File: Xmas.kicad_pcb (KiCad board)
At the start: 2 copper layers, 23 parts, among them IC1 STM32C011F6, IC2 TP4056-42, SW1 BZCN_TSA007A1518B03

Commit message: The schematic is complete
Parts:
- added C10: 100n, BornaKiCad:C0603, B.Cu at (108.2, 114.0)
- added C11: DNP, BornaKiCad:C0603, F.Cu at (79.1, 38.9)
- added C12: DNP, BornaKiCad:C0603, F.Cu at (79.1, 41.4)
- added C13: 10n, BornaKiCad:C0603, F.Cu at (79.1, 43.9)
- added C4: 100n, BornaKiCad:C0603, B.Cu at (148.1, 90.2)
- added C5: 100n, BornaKiCad:C0603, B.Cu at (112.5, 97.8)
- added C6: 100n, BornaKiCad:C0603, B.Cu at (137.3, 112.3)
- added C7: 100n, BornaKiCad:C0603, F.Cu at (79.1, 31.4)
- added C8: 10uF, BornaKiCad:C1206, F.Cu at (74.3, 41.6)
- added C9: 100n, BornaKiCad:C0603, B.Cu at (142.7, 114.2)
- added D1: BAT20JFILM, BornaKiCad:SOD323, F.Cu at (91.0, 43.7)
- added Q1: AO3401A, BornaKiCad:SOT-23-3L, F.Cu at (88.1, 47.2)
- added Q2: CJ3400, BornaKiCad:SOT-23-3L, F.Cu at (92.1, 47.2)
- added R10: 10k, BornaKiCad:R0603, B.Cu at (110.5, 113.1)
- added R11: 100k, BornaKiCad:R0603, F.Cu at (87.1, 33.9)
- added R12: 100R, BornaKiCad:R0603, F.Cu at (87.1, 36.4)
- added R13: 100k, BornaKiCad:R0603, F.Cu at (87.1, 38.9)
- added R14: 10R, BornaKiCad:R1206, F.Cu at (74.3, 44.9)
- added R4: 10k, BornaKiCad:R0603, F.Cu at (83.1, 31.4)
- added R5: 10k, BornaKiCad:R0603, F.Cu at (83.1, 33.9)
- added R6: 100R, BornaKiCad:R0603, F.Cu at (83.1, 36.4)
- added R7: 100k, BornaKiCad:R0603, F.Cu at (83.1, 38.9)
- added R8: 100k, BornaKiCad:R0603, F.Cu at (83.1, 41.4)
- added R9: 10k, BornaKiCad:R0603, B.Cu at (140.7, 113.5)
- added SPK1: MLT-7525, BornaKiCad:MTL-7525, B.Cu at (144.9, 79.8)
- added SW2: BZCN_TSA007A1518B03, BornaKiCad:TSA007A1518B03, F.Cu at (102.8, 115.3)
- added TP1: ~, BornaKiCad:TP-1_5mm, F.Cu at (90.4, 31.4)
- added TP2: ~, BornaKiCad:TP-1_5mm, F.Cu at (90.4, 33.9)
- added TP3: ~, BornaKiCad:TP-1_5mm, F.Cu at (90.4, 36.4)
- added TP4: ~, BornaKiCad:TP-1_5mm, F.Cu at (90.4, 38.9)
- added TP5: ~, BornaKiCad:TP-1_5mm, F.Cu at (90.4, 41.4)
- C1: value VALUE -> 100n; footprint BornaKiCad:C1206 -> BornaKiCad:C0603; moved to B.Cu
- C2, C3: value 2u2 -> 100n
- CONN1, CONN2, IC1: moved to B.Cu
- R1, R2: value VALUE -> 5k1
- R3: value 2k2 -> 10k
- moved SW1 79.8 mm to (147.2, 115.3), turned to -60 degrees
- moved C1 79.6 mm to (105.0, 83.0)
- moved CONN1 72.2 mm to (135.1, 97.8), turned to 90 degrees
- moved CONN2 66.5 mm to (125.0, 108.5)
- moved IC1 56.4 mm to (116.7, 83.8), turned to 180 degrees
- moved C2 8.16 mm to (48.5, 81.1)
- moved C3 4.85 mm to (53.5, 77.7)
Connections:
- net /DO renamed Net-(LED4-DO)
- net /DO2 renamed Net-(LED8-DO)
- net VBAT renamed VDD
- C1 pad 1: /DIN -> GND
- C1 pad 2: Net-(LED1-DI) -> WS_SUPPLY
- CONN2 pad A6: unconnected-(CONN2-DP1-PadA6) -> Net-(CONN2-DP1)
- CONN2 pad A7: unconnected-(CONN2-DN1-PadA7) -> Net-(CONN2-DN1)
- CONN2 pad B6: unconnected-(CONN2-DP2-PadB6) -> Net-(CONN2-DP1)
- CONN2 pad B7: unconnected-(CONN2-DN2-PadB7) -> Net-(CONN2-DN1)
- IC1 pad 12: unconnected-(IC1-PA5-Pad12) -> /BUZZER
- IC1 pad 13: unconnected-(IC1-PA6-Pad13) -> /DIN
- IC1 pad 14: unconnected-(IC1-PA7-Pad14) -> /PERIPH_SUPPLY
- IC1 pad 18: unconnected-(IC1-PA13-Pad18) -> /SW_DIO
- IC1 pad 19: unconnected-(IC1-BOOT0-Pad19) -> /SW_CLK
- IC1 pad 20: /DIN -> unconnected-(IC1-PB6-Pad20)
- IC1 pad 6: unconnected-(IC1-NRST-Pad6) -> /RST
- IC1 pad 7: unconnected-(IC1-PA0-Pad7) -> /BTN2
- IC1 pad 9: unconnected-(IC1-PA2-Pad9) -> /BTN1
- IC2 pad 1: TEMP -> Net-(IC2-TEMP)
- IC2 pad 2: PROG -> Net-(IC2-PROG)
- LED1 pad 3: Net-(LED1-DI) -> /DIN
- LED1 pad 4: unconnected-(LED1-VDD-Pad4) -> WS_SUPPLY
- LED10 pad 4: unconnected-(LED10-VDD-Pad4) -> WS_SUPPLY
- LED11 pad 4: unconnected-(LED11-VDD-Pad4) -> WS_SUPPLY
- LED12 pad 4: unconnected-(LED12-VDD-Pad4) -> WS_SUPPLY
- LED2 pad 4: unconnected-(LED2-VDD-Pad4) -> WS_SUPPLY
- LED3 pad 4: unconnected-(LED3-VDD-Pad4) -> WS_SUPPLY
- LED4 pad 4: unconnected-(LED4-VDD-Pad4) -> WS_SUPPLY
- LED5 pad 4: unconnected-(LED5-VDD-Pad4) -> WS_SUPPLY
- LED6 pad 4: unconnected-(LED6-VDD-Pad4) -> WS_SUPPLY
- LED7 pad 4: unconnected-(LED7-VDD-Pad4) -> WS_SUPPLY
- LED8 pad 4: unconnected-(LED8-VDD-Pad4) -> WS_SUPPLY
- LED9 pad 4: unconnected-(LED9-VDD-Pad4) -> WS_SUPPLY
- SW1 pad 1: unconnected-(SW1-SW1-Pad1) -> GND
- SW1 pad 2: unconnected-(SW1-SW2-Pad2) -> /BTN1
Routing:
- net /BTN1: track 0.00 -> 65.8 mm, vias 0 -> 2
- net /BTN2: track 0.00 -> 54.0 mm, vias 0 -> 2
- net Net-(LED3-DO): track 50.2 -> 26.2 mm, vias 0 -> 2
- net GND: track 0.00 -> 21.0 mm, vias 0 -> 4
- net WS_SUPPLY: track 0.00 -> 18.7 mm, vias 0 -> 4
- net Net-(LED10-DI): track 18.5 -> 25.7 mm, vias 0 -> 2
- net Net-(LED11-DO): track 35.2 -> 29.7 mm
- net Net-(LED7-DO): track 30.1 -> 26.7 mm
- net Net-(LED6-DO): track 56.3 -> 53.3 mm, vias 0 -> 4
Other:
- board outline added: 50 x 60.6 mm

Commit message: Update PCB
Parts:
- moved CONN2 5.55 mm to (130.5, 109.1), turned to 180 degrees
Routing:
- net Net-(LED3-DO): track 26.2 -> 45.2 mm, vias 2 -> 4
- net /BTN1: track 65.8 -> 58.0 mm, vias 2 -> 1
- net /BTN2: track 54.0 -> 49.3 mm, vias 2 -> 1
- net GND: track 21.0 -> 19.2 mm
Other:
- outline, holes or cut-outs redrawn

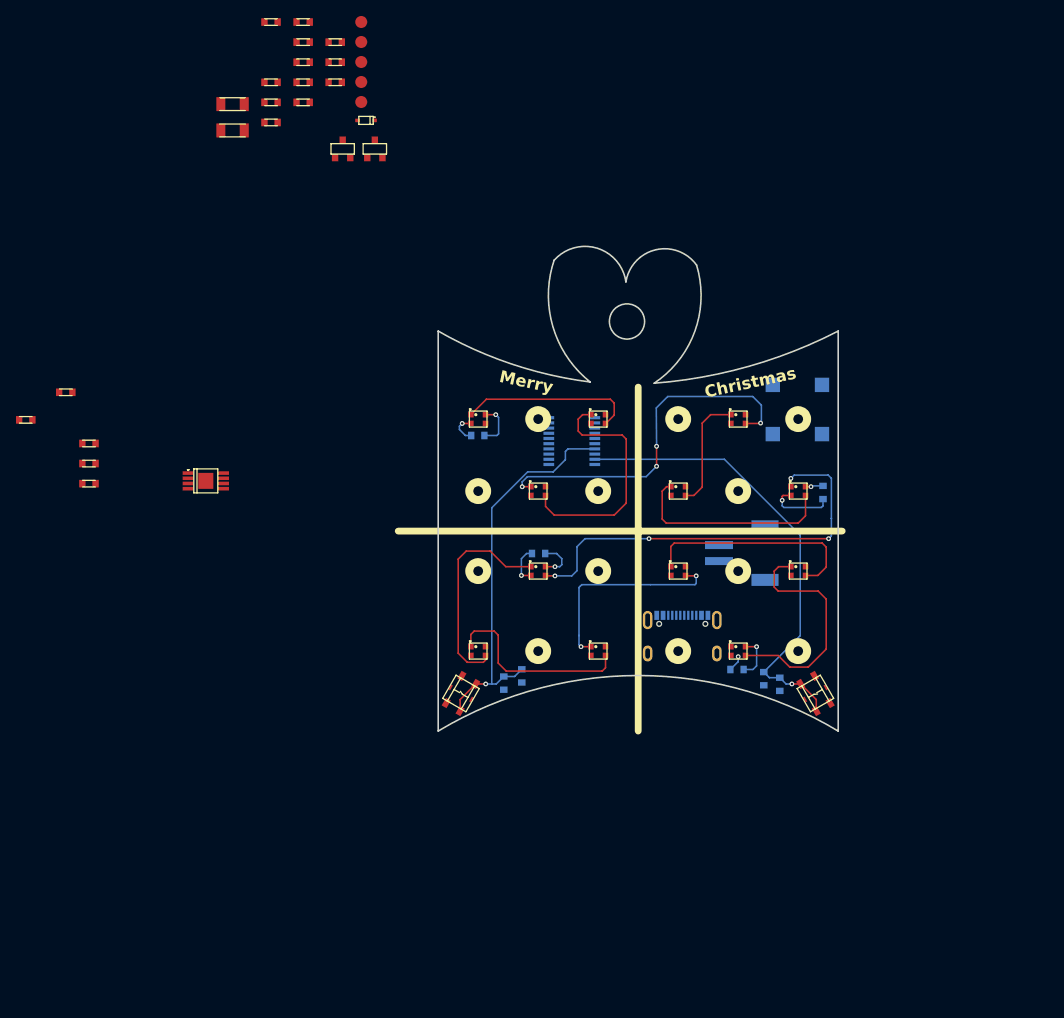
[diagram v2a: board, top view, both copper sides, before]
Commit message: Everything on the PCB is connected
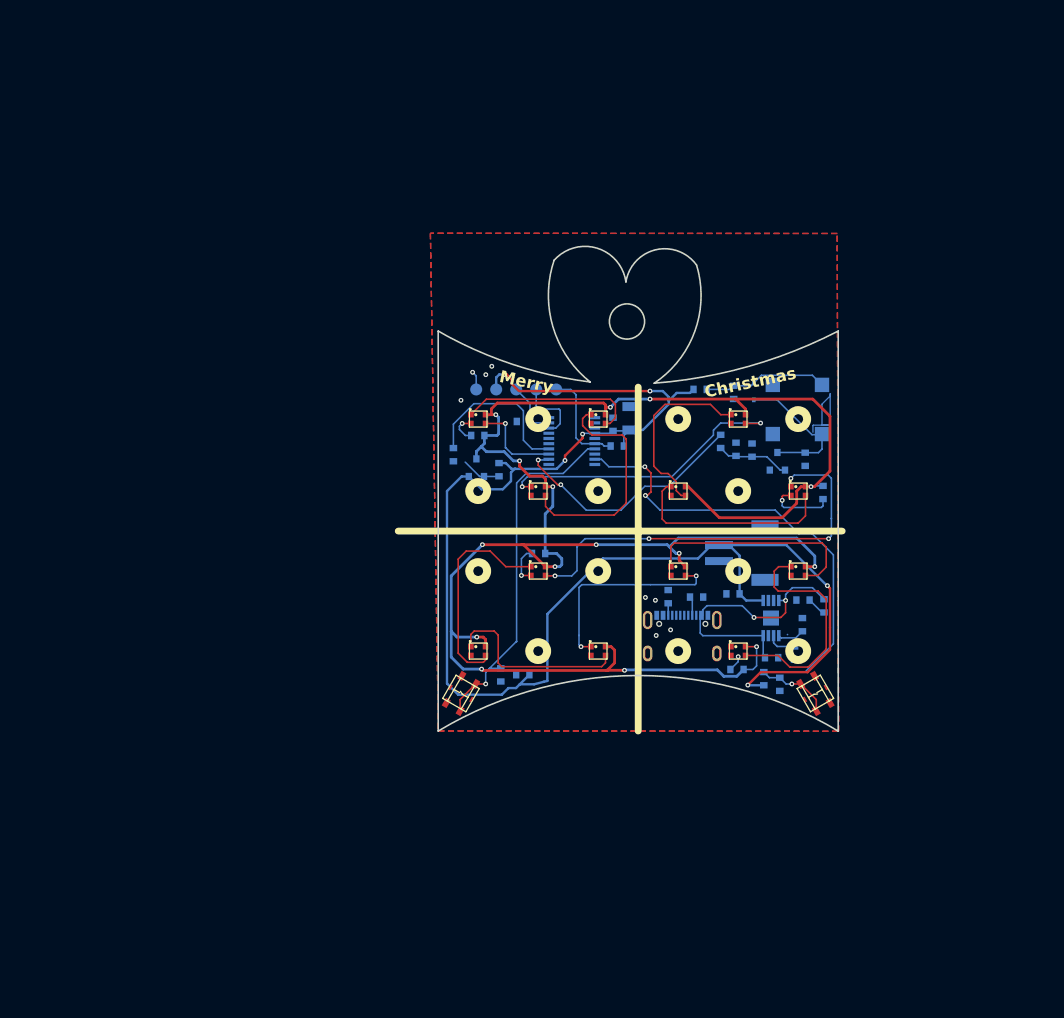
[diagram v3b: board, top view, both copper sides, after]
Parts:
- added LED13: ~, BornaKiCad:LED_0603, B.Cu at (148.2, 104.4)
- C11, C12, C13, C2, C3, C7, C8, D1, IC2, Q1, Q2, R1, R11, R12, R13, R2, R3, R4, R5, R6, R7, R8, TP1, TP2, TP3, TP4, TP5: moved to B.Cu
- R14: footprint BornaKiCad:R1206 -> BornaKiCad:R0603; moved to B.Cu
- moved R4 100.0 mm to (144.6, 110.2), turned to 90 degrees
- moved C2 97.8 mm to (141.7, 110.8), turned to 180 degrees
- moved R5 95.9 mm to (145.5, 106.7), turned to -90 degrees
- moved R3 90.4 mm to (145.6, 103.6)
- moved C3 87.1 mm to (136.8, 102.8)
- moved C12 80.3 mm to (145.9, 86.0), turned to 90 degrees
- moved R1 78.3 mm to (132.3, 103.2)
- moved R2 74.3 mm to (128.8, 103.2), turned to 90 degrees
- moved C11 74.0 mm to (137.2, 84.8), turned to -90 degrees
- moved IC2 72.7 mm to (141.6, 105.9), turned to 90 degrees
- moved R13 69.5 mm to (139.2, 84.9), turned to -90 degrees
- moved R12 67.6 mm to (135.3, 83.8), turned to -90 degrees
- moved C13 66.9 mm to (136.9, 77.7), turned to 90 degrees
- moved R14 66.8 mm to (132.7, 77.3), turned to 180 degrees
- moved C7 66.0 mm to (121.8, 81.7), turned to -90 degrees
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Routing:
- net WS_SUPPLY: track 18.7 -> 238.2 mm, vias 4 -> 15
- net VDD: track 0.00 -> 190.7 mm, vias 0 -> 6
- net VUSB: track 0.00 -> 34.1 mm, vias 0 -> 2
- net /BUZZER: track 0.00 -> 31.1 mm, vias 0 -> 2
- net Net-(Q2-D): track 0.00 -> 20.6 mm
- net /PERIPH_SUPPLY: track 0.00 -> 20.5 mm
- net Net-(C13-Pad2): track 0.00 -> 15.9 mm
- net (no net): track 0.00 -> 12.9 mm
- net /RST: track 0.00 -> 12.9 mm
- net /DIN: track 0.00 -> 11.3 mm, vias 0 -> 1
- net /BTN1: track 58.0 -> 68.5 mm, vias 1 -> 3
- net Net-(Q2-G): track 0.00 -> 9.18 mm
- net Net-(LED4-DO): track 14.5 -> 23.2 mm
- net /SW_DIO: track 0.00 -> 8.61 mm
- net Net-(LED3-DO): track 45.2 -> 36.9 mm, vias 4 -> 2
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- added copper zone on B.Cu, net GND
- added copper zone on F.Cu, net GND

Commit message: Update PCB
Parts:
- moved R10 8.09 mm to (103.2, 109.8)
- moved R9 7.77 mm to (147.7, 110.0), turned to 90 degrees
- moved LED13 3.65 mm to (145.6, 101.9), turned to 0 degrees
- moved R6 3.04 mm to (104.8, 84.7), turned to 0 degrees
- moved C10 2.82 mm to (105.2, 112.0), turned to 180 degrees
- moved R12 2.07 mm to (134.3, 85.6), turned to 0 degrees
- moved C9 1.40 mm to (142.6, 112.8), turned to 0 degrees
- moved R11 0.66 mm to (108.2, 87.2), turned to -90 degrees
- moved Q1 0.40 mm to (105.2, 87.2), turned to -90 degrees
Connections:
- IC1 pad 11: unconnected-(IC1-PA4-Pad11) -> /BTN2
- IC1 pad 7: /BTN2 -> unconnected-(IC1-PA0-Pad7)
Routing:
- net VDD: track 190.7 -> 163.0 mm, vias 6 -> 2
- net WS_SUPPLY: track 238.2 -> 213.8 mm, vias 15 -> 13
- net /BUZZER: track 31.1 -> 25.9 mm
- net /BTN1: track 68.5 -> 63.8 mm
- net VUSB: track 34.1 -> 29.8 mm
- net Net-(Q1-G): track 4.98 -> 1.79 mm
- net /BTN2: track 45.5 -> 43.6 mm
- net Net-(Q2-D): track 20.6 -> 21.7 mm
- net /RST: track 12.9 -> 11.8 mm
- net GND: track 21.5 -> 20.6 mm, vias 12 -> 57
- net Net-(LED3-DO): track 36.9 -> 36.2 mm
- net Net-(LED11-DO): track 29.3 -> 28.6 mm
- net Net-(LED13-K): track 2.44 -> 1.76 mm
- net /PERIPH_SUPPLY: track 20.5 -> 21.1 mm

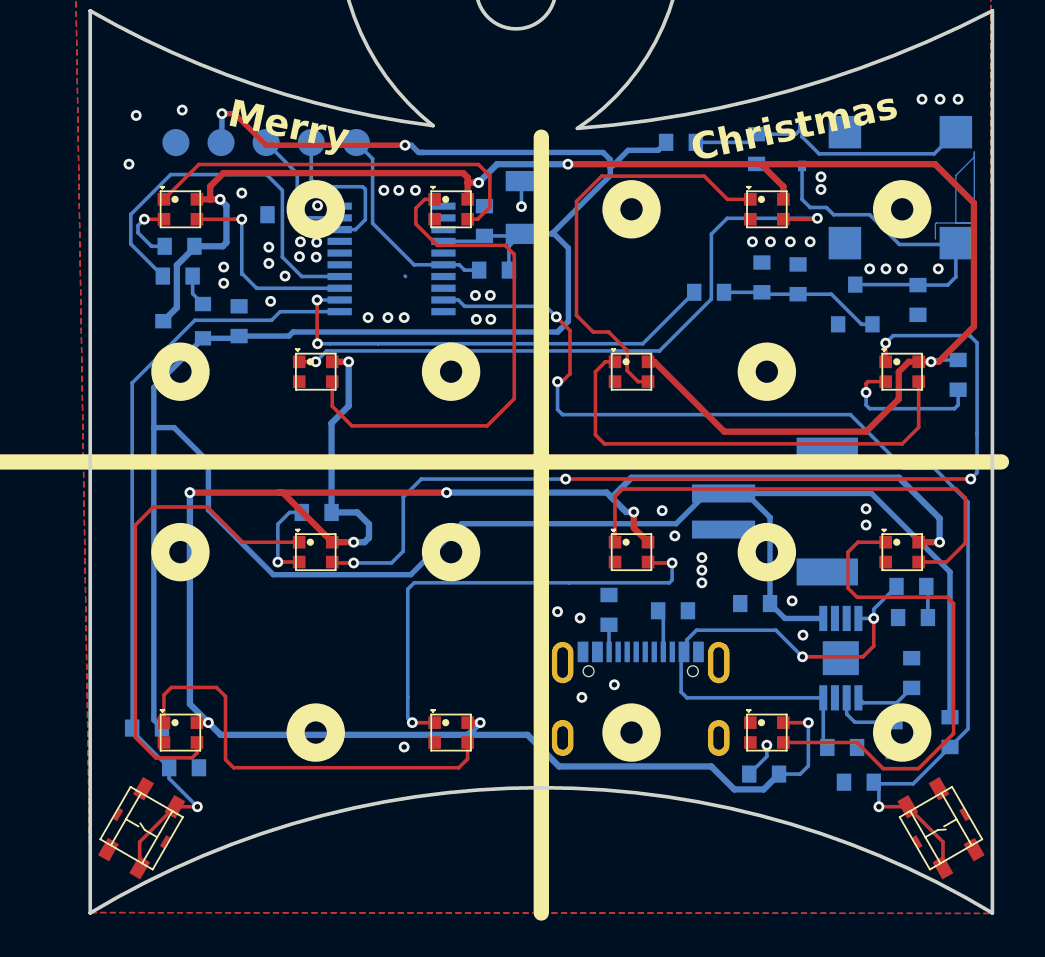
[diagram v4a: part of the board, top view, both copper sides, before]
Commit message: Connected uncotected traces/Marina
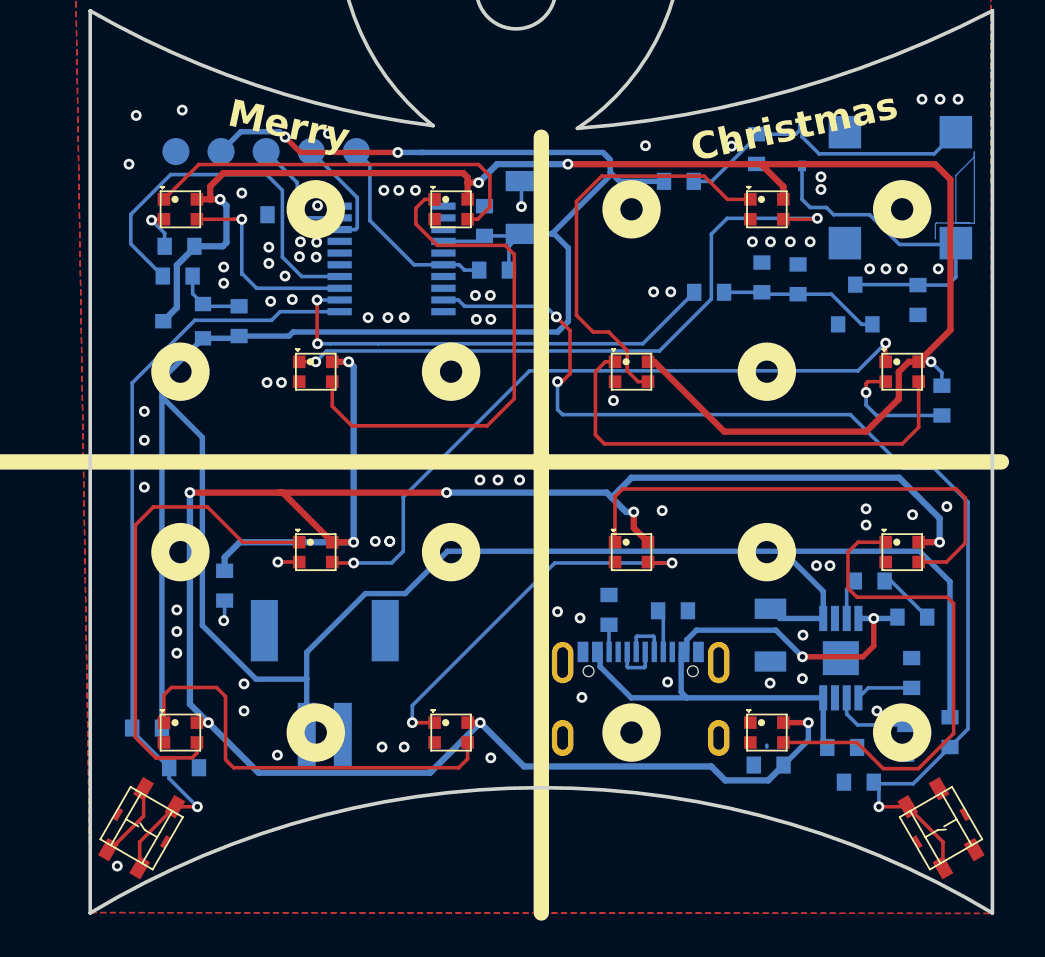
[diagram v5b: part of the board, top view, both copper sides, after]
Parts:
- C3: value 100n -> 10u; footprint BornaKiCad:C0603 -> Borna KiCAD Library:C1206
- moved CONN1 25.3 mm to (113.0, 110.1), turned to 180 degrees
- moved C5 6.52 mm to (107.5, 101.9), turned to 90 degrees
- moved R3 3.14 mm to (143.2, 101.6)
- moved R14 2.16 mm to (132.6, 79.5)
- moved C3 1.95 mm to (137.7, 104.6), turned to 90 degrees
- moved LED13 1.70 mm to (145.6, 103.6)
- moved C4 1.69 mm to (147.2, 91.6)
- moved R4 0.67 mm to (145.2, 110.4)
- moved C6 0.56 mm to (137.6, 111.8)
- moved TP1 0.50 mm to (104.8, 77.8)
- moved TP2 0.50 mm to (107.2, 77.8)
- moved TP3 0.50 mm to (109.8, 77.8)
- moved TP4 0.50 mm to (112.2, 77.8)
- moved TP5 0.50 mm to (114.8, 77.8)
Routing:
- net Net-(LED6-DO): track 53.3 -> 38.5 mm, vias 4 -> 2
- net VUSB: track 29.8 -> 35.2 mm
- net VDD: track 163.0 -> 167.8 mm
- net Net-(LED10-DI): track 25.7 -> 21.2 mm
- net WS_SUPPLY: track 213.8 -> 217.7 mm
- net GND: track 20.6 -> 17.2 mm, vias 57 -> 86
- net Net-(CONN2-DN1): track 0.00 -> 2.68 mm
- net Net-(CONN2-DP1): track 0.00 -> 2.68 mm
- net /SW_DIO: track 8.61 -> 6.30 mm
- net Net-(IC2-CHRG): track 0.00 -> 2.26 mm
- net Net-(Q1-G): track 1.79 -> 3.84 mm
- net Net-(LED13-K): track 1.76 -> 3.19 mm
- net Net-(C13-Pad2): track 16.4 -> 17.4 mm
- net Net-(IC2-PROG): track 3.71 -> 4.42 mm
- net /RST: track 11.8 -> 11.3 mm
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
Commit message: Fixed paths in project files.
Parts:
- C1, C10, C11, C12, C13, C2, C4, C5, C6, C7, C9: footprint BornaKiCad:C0603 -> Borna KiCAD Library:C0603
- C8: footprint BornaKiCad:C1206 -> Borna KiCAD Library:C1206
- CONN1: footprint BornaKiCad:JST_S2B-PH-SM4-TB -> Borna KiCAD Library:JST_S2B-PH-SM4-TB
- CONN2: footprint BornaKiCad:TYPE-C_16PIN_2MD(073) -> Borna KiCAD Library:TYPE-C_16PIN_2MD(073)
- D1: footprint BornaKiCad:SOD323 -> Borna KiCAD Library:SOD323
- IC1: footprint BornaKiCad:TSSOP20 -> Borna KiCAD Library:TSSOP20
- IC2: footprint BornaKiCad:EMSOP -> Borna KiCAD Library:EMSOP
- LED1, LED10, LED11, LED12, LED2, LED3, LED4, LED5, LED6, LED7, LED8, LED9: footprint BornaKiCad:WS2812B-2020 -> Borna KiCAD Library:WS2812B-2020
- LED13: footprint BornaKiCad:LED_0603 -> Borna KiCAD Library:LED_0603
- Q1, Q2: footprint BornaKiCad:SOT-23-3L -> Borna KiCAD Library:SOT-23-3L
- R1, R10, R11, R12, R13, R14, R2, R3, R4, R5, R6, R7, R8, R9: footprint BornaKiCad:R0603 -> Borna KiCAD Library:R0603
- SPK1: footprint BornaKiCad:MTL-7525 -> Borna KiCAD Library:MTL-7525
- SW1, SW2: footprint BornaKiCad:TSA007A1518B03 -> Borna KiCAD Library:TSA007A1518B03
- TP1, TP2, TP3, TP4, TP5: footprint BornaKiCad:TP-1_5mm -> Borna KiCAD Library:TP-1_5mm
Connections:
- SW1 pad PAD: unconnected-(SW1-PadPAD) -> GND
- SW2 pad PAD: unconnected-(SW2-PadPAD) -> GND
